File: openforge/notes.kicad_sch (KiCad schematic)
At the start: 0 parts

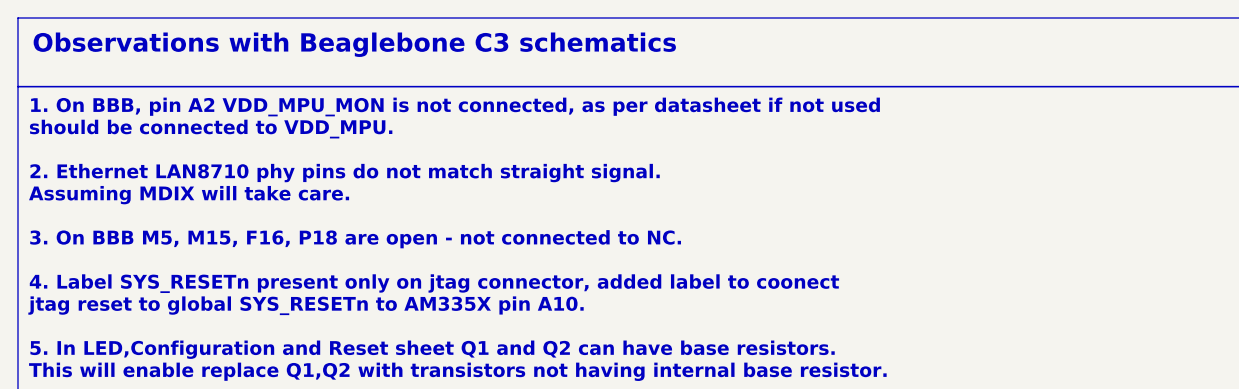
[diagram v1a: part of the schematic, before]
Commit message: Completed footprint association. Partially placed top side components on PCB
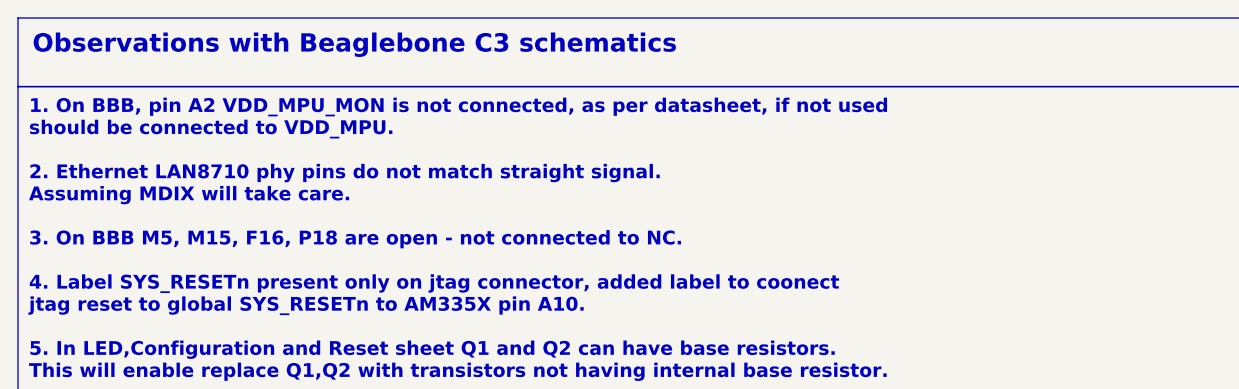
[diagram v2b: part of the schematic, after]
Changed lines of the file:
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@@
 		)
 	)
-	(text_box "1. On BBB, pin A2 VDD_MPU_MON is not connected, as per datasheet if not used\n   should be connected to VDD_MPU.\n\n2. Ethernet LAN8710 phy pins do not match straight signal.\n   Assuming MDIX will take care.\n\n3. On BBB M5, M15, F16, P18 are open - not connected to NC.\n\n4. Label SYS_RESETn present only on jtag connector, added label to coonect\n   jtag reset to global SYS_RESETn to AM335X pin A10.\n\n5. In LED,Configuration and Reset sheet Q1 and Q2 can have base resistors.\n   This will enable replace Q1,Q2 with transistors not having internal base resistor."
+	(text_box "1. On BBB, pin A2 VDD_MPU_MON is not connected, as per datasheet, if not used\n   should be connected to VDD_MPU.\n\n2. Ethernet LAN8710 phy pins do not match straight signal.\n   Assuming MDIX will take care.\n\n3. On BBB M5, M15, F16, P18 are open - not connected to NC.\n\n4. Label SYS_RESETn present only on jtag connector, added label to coonect\n   jtag reset to global SYS_RESETn to AM335X pin A10.\n\n5. In LED,Configuration and Reset sheet Q1 and Q2 can have base resistors.\n   This will enable replace Q1,Q2 with transistors not having internal base resistor."
 		(exclude_from_sim no)
 		(at 40.64 35.56 0)
